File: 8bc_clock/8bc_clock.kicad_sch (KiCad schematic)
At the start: 25 parts, among them J1 Conn_01x05_Pin, SW1 SW_SPDT, SW2 SW_DIP_x01, U1 ICM7555xP, U2 ICM7555xP, U3 ICM7555xP, U4 74LS04, U5 74LS08, U6 74LS32

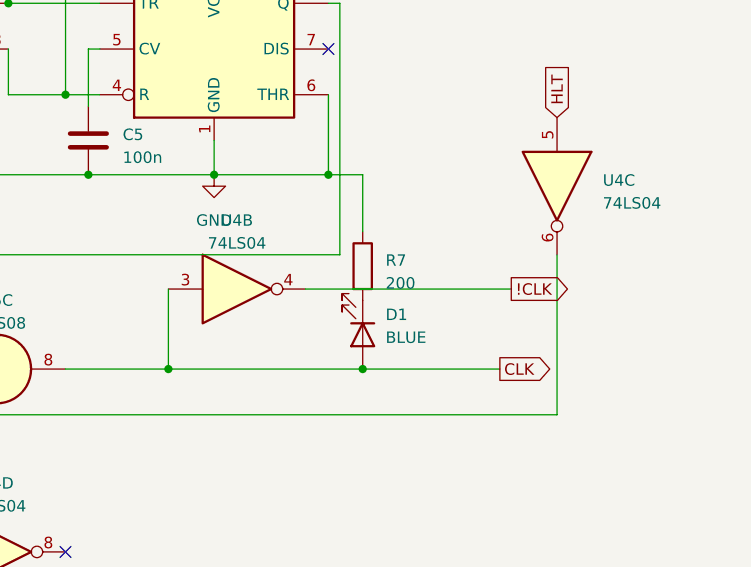
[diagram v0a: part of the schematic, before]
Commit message: fixed R value
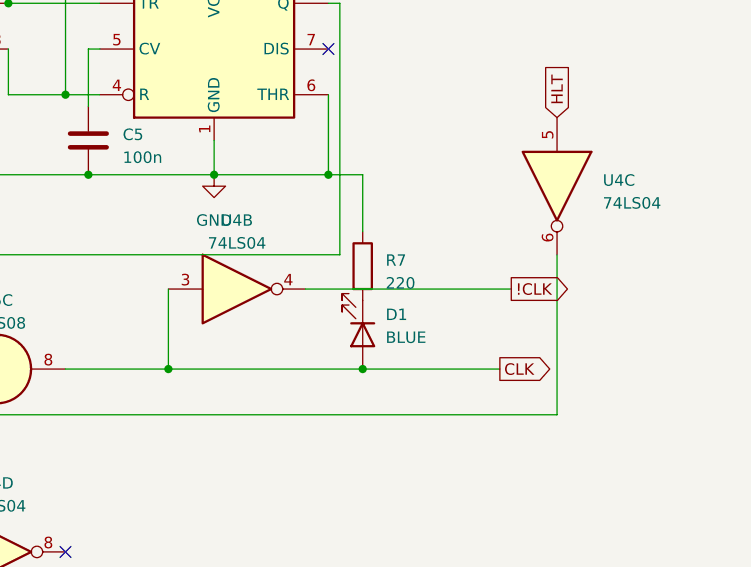
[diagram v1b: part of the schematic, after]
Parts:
- R7: value 200 -> 220
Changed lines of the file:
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@@
       (effects (font (size 1.27 1.27)) (justify left))
     )
-    (property "Value" "200" (at 198.12 92.075 0)
+    (property "Value" "220" (at 198.12 92.075 0)
       (effects (font (size 1.27 1.27)) (justify left))
     )

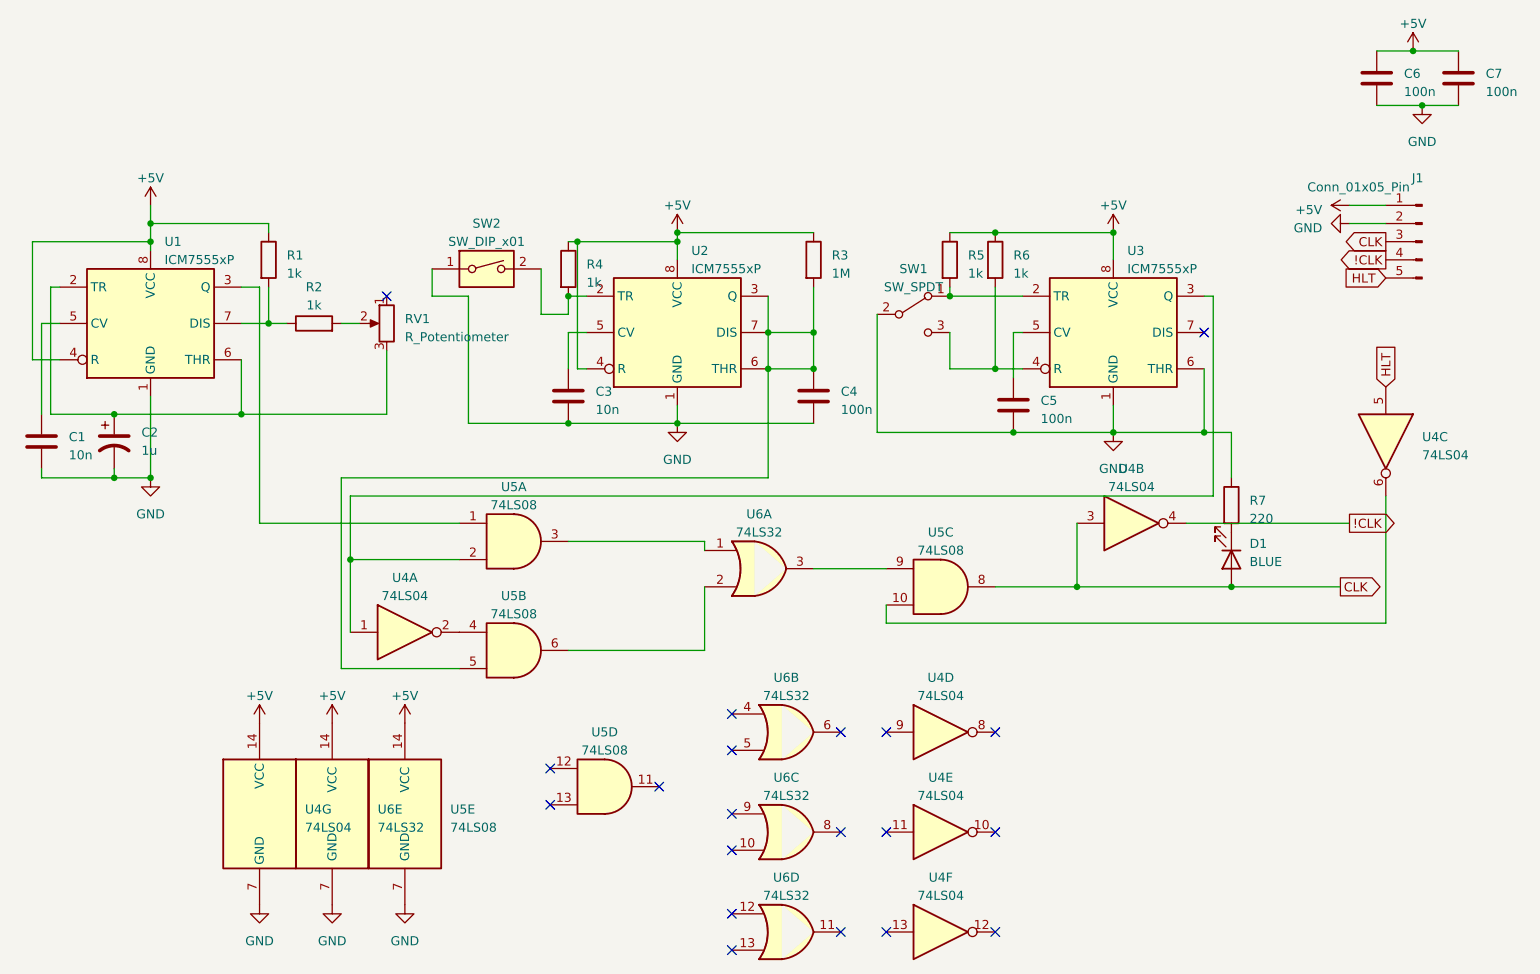
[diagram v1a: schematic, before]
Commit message: fixed clock circuit error
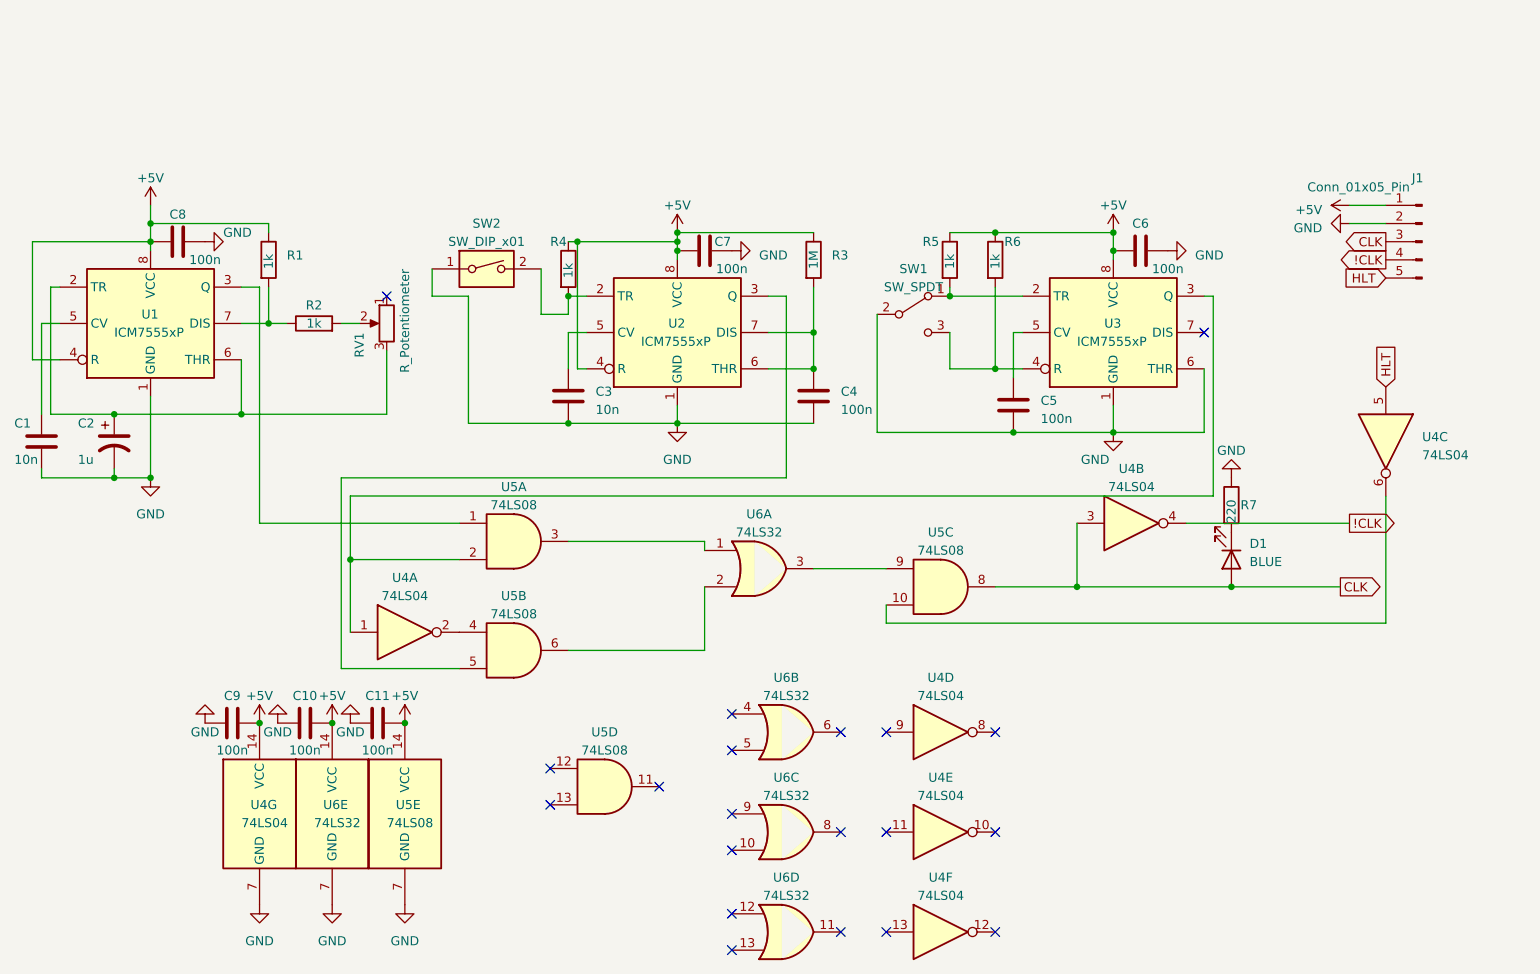
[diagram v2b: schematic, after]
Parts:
- added C10, C11, C8, C9: 100n, Capacitor_THT:C_Radial_D8.0mm_H7.0mm_P3.50mm, symbol Device:C
- R1, R2: footprint Resistor_THT:R_Axial_DIN0204_L3.6mm_D1.6mm_P7.62mm_Horizontal -> Resistor_THT:R_Axial_DIN0207_L6.3mm_D2.5mm_P7.62mm_Horizontal
- R7: footprint Resistor_THT:R_Axial_DIN0207_L6.3mm_D2.5mm_P10.16mm_Horizontal -> Resistor_THT:R_Axial_DIN0207_L6.3mm_D2.5mm_P7.62mm_Horizontal
- RV1: footprint Potentiometer_THT:Potentiometer_Alpha_RD901F-40-00D_Single_Vertical -> Potentiometer_THT:Potentiometer_Bourns_PTV09A-1_Single_Vertical
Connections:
- net +5V: now also C7.1, C10.2, C11.2, C8.1, C9.2; no longer C7.2
- net GND: now also C7.2, C10.1, C11.1, C8.2, C9.1; no longer C7.1
- net at C4.1, R3.2, U2.6 (THR)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: no longer U2.3 (Q), U5.5
- new net: U2.3 (Q), U5.5
